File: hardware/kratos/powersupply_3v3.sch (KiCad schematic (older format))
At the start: 1 part, among them U4 AP2138

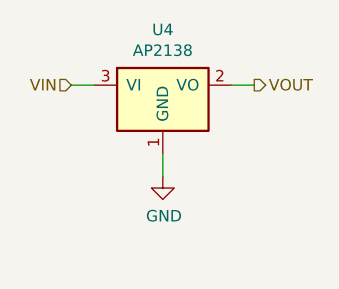
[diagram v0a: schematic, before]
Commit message: Update to linear regulators. Added PCB layout
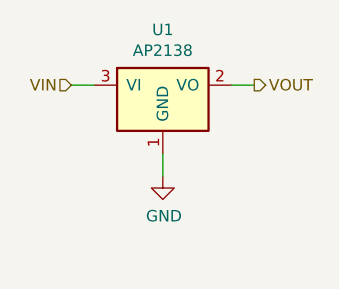
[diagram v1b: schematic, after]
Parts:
- renumbered U4 to U1
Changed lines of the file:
@@
 $Descr A4 11693 8268
 encoding utf-8
-Sheet 5 6
-Title ""
-Date ""
-Rev "REVA"
+Sheet 2 6
+Title "3.3V Power Supply"
+Date "2021-03-13"
+Rev "A"
 Comp ""
 Comment1 "Author: Natesh Narain"
@@
 $EndDescr
 $Comp
-L linear_regulators:AP2138 U4
+L linear_regulators:AP2138 U1
 U 1 1 6042BAC0
 P 5550 2950
-F 0 "U4" H 5550 3042 50  0000 C CNN
+F 0 "U1" H 5550 3042 50  0000 C CNN
 F 1 "AP2138" H 5550 2951 50  0000 C CNN
 F 2 "Package_TO_SOT_SMD:SOT-23" H 6300 2950 50  0001 C CNN
@@
 Text HLabel 5150 3100 0    50   Input ~ 0
 VIN
-Text HLabel 5950 3100 2    50   Output ~ 0
-VOUT
 $Comp
-L power:GND #PWR026
+L power:GND #PWR09
 U 1 1 6042BE0A
 P 5550 3500
-F 0 "#PWR026" H 5550 3250 50  0001 C CNN
+F 0 "#PWR09" H 5550 3250 50  0001 C CNN
 F 1 "GND" H 5555 3327 50  0000 C CNN
 F 2 "" H 5550 3500 50  0001 C CNN
@@
 Wire Wire Line
 	5850 3100 5950 3100
+Text HLabel 5950 3100 2    50   Output ~ 0
+VOUT
 $EndSCHEMATC

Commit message: Update digikey part numbers in schematics
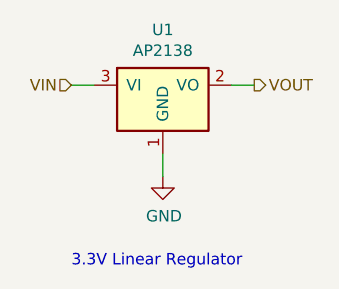
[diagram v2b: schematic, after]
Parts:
- U1: Digi-Key_PN (none) -> AP2138N-3.3TRG1DITR-ND
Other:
- note added: "3.3V Linear Regulator\n"
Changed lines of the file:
@@
 F 2 "Package_TO_SOT_SMD:SOT-23" H 6300 2950 50  0001 C CNN
 F 3 "https://www.diodes.com/assets/Datasheets/AP2138-9.pdf" H 5550 3050 50  0001 C CNN
+F 4 "AP2138N-3.3TRG1DITR-ND" H 5550 2950 50  0001 C CNN "Digi-Key_PN"
 	1    5550 2950
 	1    0    0    -1
@@
 Text HLabel 5950 3100 2    50   Output ~ 0
 VOUT
+Text Notes 5150 3900 0    50   ~ 0
+3.3V Linear Regulator\n
 $EndSCHEMATC
